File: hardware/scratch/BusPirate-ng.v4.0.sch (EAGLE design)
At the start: 133 parts, among them IC1 IC_MEM_23LC1024, IC10 IC_BUFF_SN74LVC1T45DBV, IC11 IC_BUFF_SN74LVC1T45DBV, IC12 74LVC1G07DBV, IC13 IC_BUFF_SN74LVC1T45DBV, IC14 IC_BL1551, IC15 IC_BL1551, IC16 74HCT4066PW, IC2 IC_MEM_23LC1024, IC3 IC_74AC573, IC4 74LVC1G07DBV, IC5 74LVC1G07DBV, IC6 74LVC1G07DBV, IC7 74LVC1G07DBV, IC8 IC_BUFF_SN74LVC1T45DBV, IC9 IC_BUFF_SN74LVC1T45DBV, J1 CON_HEADER_2X02-PTH, J2 CON_HEADER_1X04, J3 CON_HEADER_1X03-PTH, J4 CON_HEADER_1X10-RIGHT_ANGLED_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, U1 IC_MEM_AT45DB041D, U2 IC_UC_STM32F103ZX, U3 IC_FPGA_ICE40HX4K

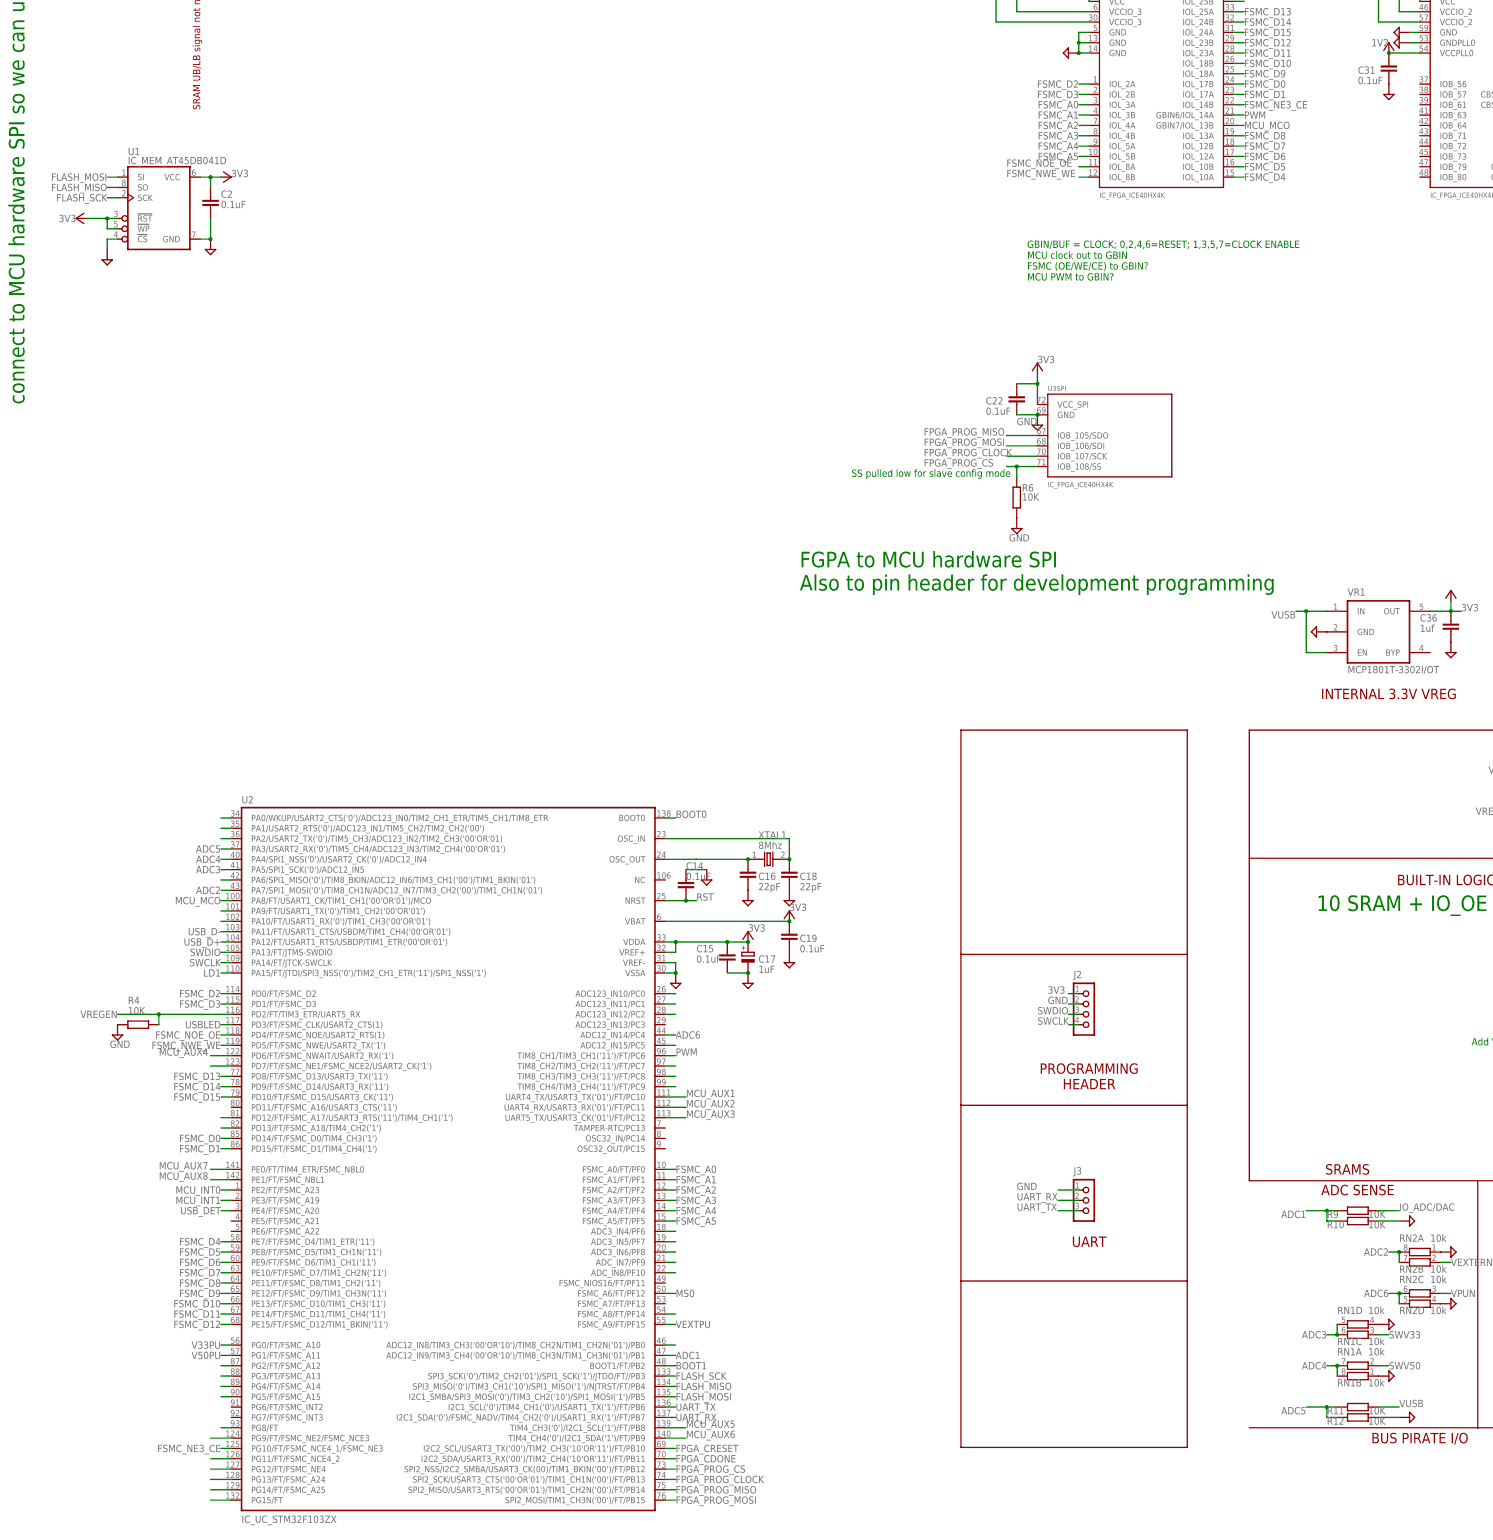
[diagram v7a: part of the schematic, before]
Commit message: added new aux pins connecting MCU to FPGA, created gerbers for BP ultra and BP ultra testboard
Moved pins to make way for AUX pins connection
-swapped MCU pins PB10(FPGA_CRESET) and PB11(FPGA_CDONE)
-moved VREGEN from MCU pin PD2 to PF14

New aux pins connecting MCU to FPGA
-MCU_AUX9 FPGA_37 PF13
-MCU_AUX10 FPGA_38 PB0
-MCU_AUX11 FPGA_39 PC5
-MCU_AUX12 FPGA_41 PA6
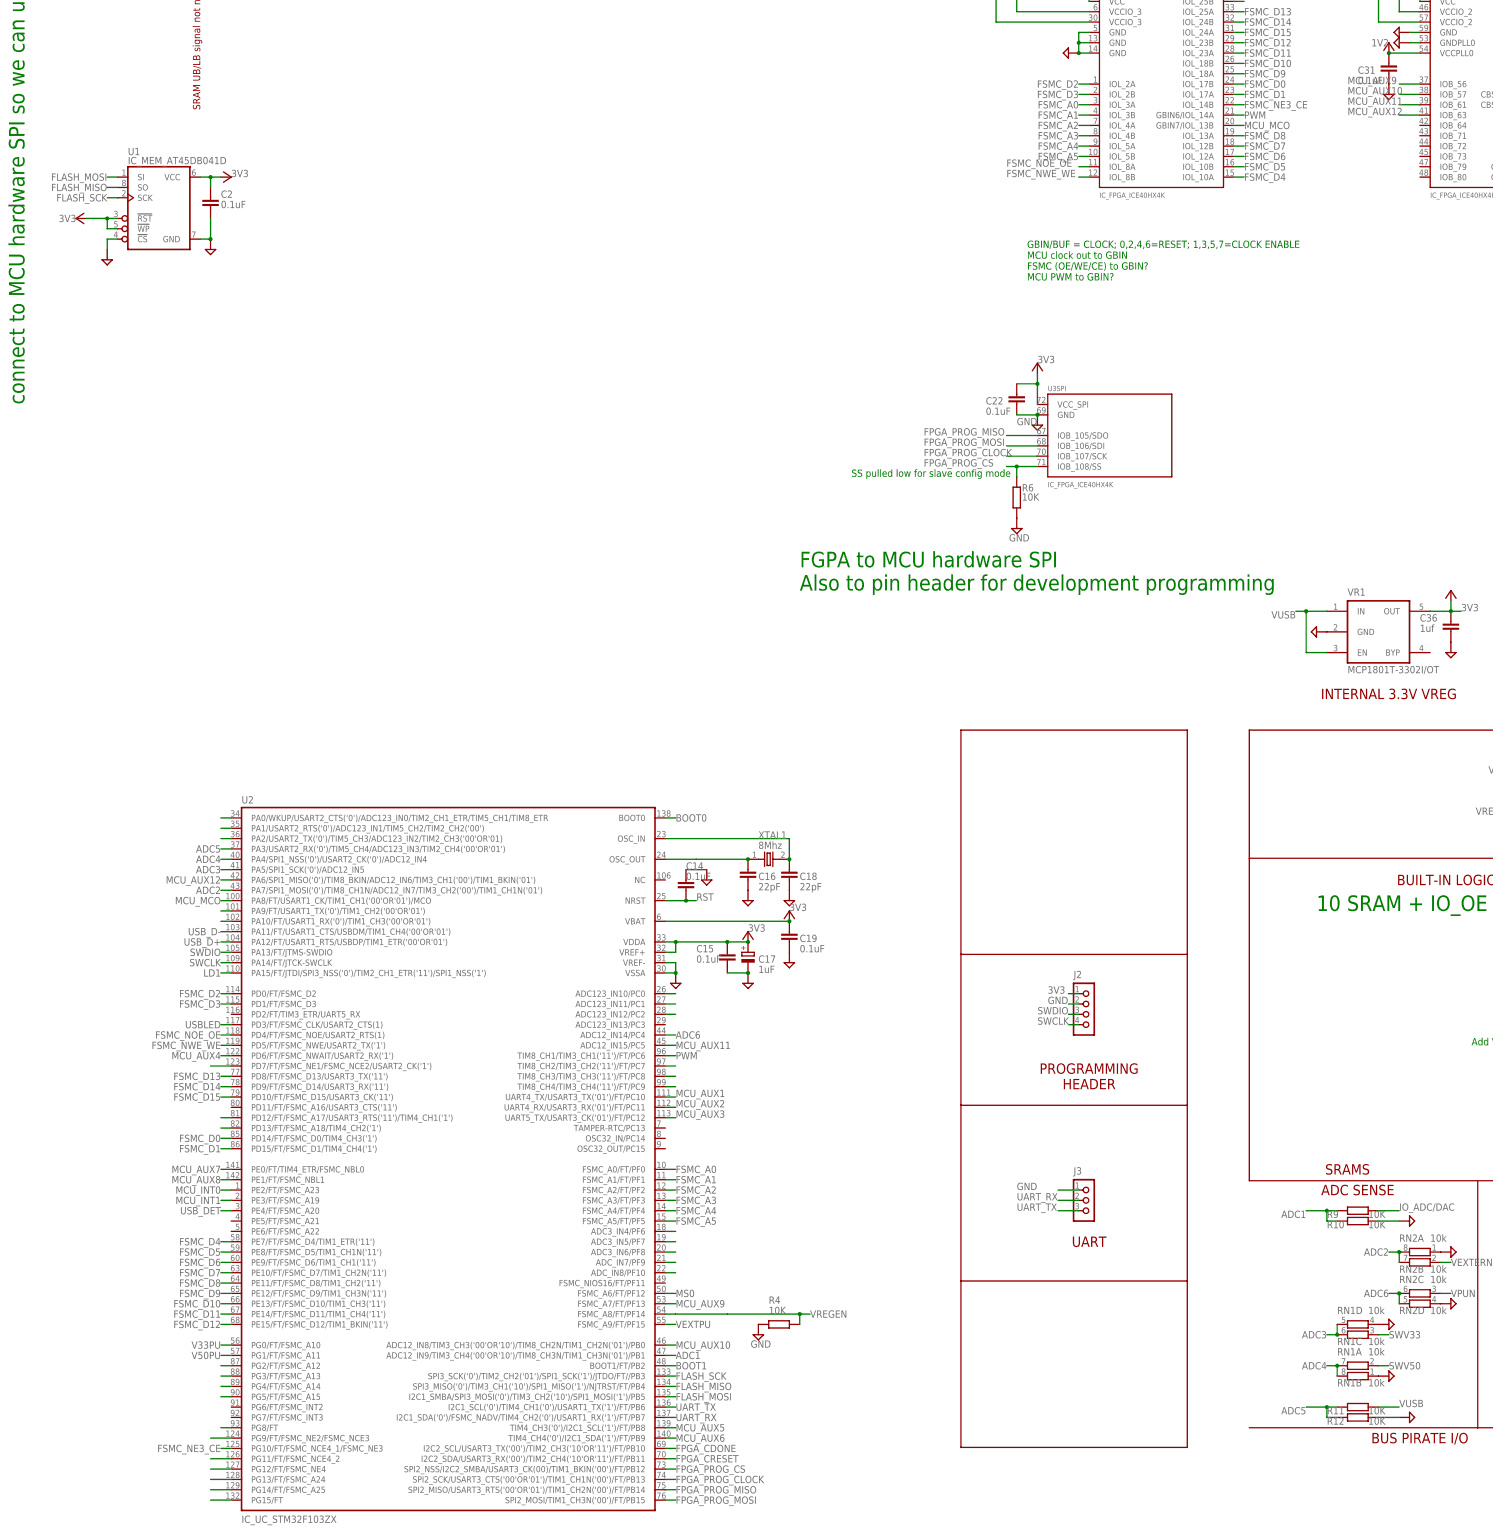
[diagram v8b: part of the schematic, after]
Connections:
- removed net N$15: U2U.FSMC_A8/FT/PF14
- removed net N$25: U2U.ADC12_IN15/PC5
- removed net N$42: U2U.PA6/SPI1_MISO('0')/TIM8_BKIN/ADC12_IN6/TIM3_CH1('00')/TIM1_BKIN('01')
- removed net N$44: U2U.ADC12_IN8/TIM3_CH3('00'OR'10')/TIM8_CH2N/TIM1_CH2N('01')/PB0
- new net MCU_AUX10: U2U.ADC12_IN8/TIM3_CH3('00'OR'10')/TIM8_CH2N/TIM1_CH2N('01')/PB0, U3BANK2.IOB_57
- new net MCU_AUX11: U2U.ADC12_IN15/PC5, U3BANK2.IOB_61
- new net MCU_AUX12: U2U.PA6/SPI1_MISO('0')/TIM8_BKIN/ADC12_IN6/TIM3_CH1('00')/TIM1_BKIN('01'), U3BANK2.IOB_63
- new net MCU_AUX9: U2U.FSMC_A7/FT/PF13, U3BANK2.IOB_56
- net FPGA_CDONE: now also U2U.I2C2_SCL/USART3_TX('00')/TIM2_CH3('10'OR'11')/FT/PB10; no longer U2U.I2C2_SDA/USART3_RX('00')/TIM2_CH4('10'OR'11')/FT/PB11
- net FPGA_CRESET: now also U2U.I2C2_SDA/USART3_RX('00')/TIM2_CH4('10'OR'11')/FT/PB11; no longer U2U.I2C2_SCL/USART3_TX('00')/TIM2_CH3('10'OR'11')/FT/PB10
- net VREGEN: now also U2U.FSMC_A8/FT/PF14; no longer U2U.PD2/FT/TIM3_ETR/UART5_RX
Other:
- moved on the sheet: R4
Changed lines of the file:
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@@
 <instance part="SUPPLY13" gate="GND" x="-121.92" y="149.86" smashed="yes"/>
 <instance part="SUPPLY9" gate="GND" x="-139.7" y="149.86" smashed="yes"/>
-<instance part="R4" gate="G$1" x="-271.78" y="139.7" smashed="yes" rot="R180">
-<attribute name="NAME" x="-274.32" y="144.78" size="1.778" layer="95"/>
-<attribute name="VALUE" x="-274.32" y="142.24" size="1.778" layer="96"/>
+<instance part="R4" gate="G$1" x="-114.3" y="66.04" smashed="yes" rot="R180">
+<attribute name="NAME" x="-116.84" y="71.12" size="1.778" layer="95"/>
+<attribute name="VALUE" x="-116.84" y="68.58" size="1.778" layer="96"/>
 </instance>
-<instance part="SUPPLY5" gate="GND" x="-276.86" y="137.16"/>
+<instance part="SUPPLY5" gate="GND" x="-119.38" y="63.5"/>
 <instance part="J4" gate="J" x="243.84" y="304.8" rot="MR180"/>
 <instance part="C31" gate="G$1" x="35.56" y="373.38" smashed="yes" rot="R180">
@@
 </segment>
 <segment>
-<label x="-276.86" y="142.24" size="1.778" layer="95" align="center-right"/>
+<label x="-106.68" y="68.58" size="1.778" layer="95" align="center-left"/>
 <pinref part="R4" gate="G$1" pin="1"/>
-<wire x1="-266.7" y1="142.24" x2="-276.86" y2="142.24" width="0.1524" layer="91"/>
-<wire x1="-266.7" y1="139.7" x2="-266.7" y2="142.24" width="0.1524" layer="91"/>
-<pinref part="U2" gate="U" pin="PD2/FT/TIM3_ETR/UART5_RX"/>
-<wire x1="-266.7" y1="142.24" x2="-248.92" y2="142.24" width="0.1524" layer="91"/>
-<junction x="-266.7" y="142.24"/>
+<wire x1="-109.22" y1="68.58" x2="-127" y2="68.58" width="0.1524" layer="91"/>
+<wire x1="-109.22" y1="66.04" x2="-109.22" y2="68.58" width="0.1524" layer="91"/>
+<wire x1="-109.22" y1="68.58" x2="-106.68" y2="68.58" width="0.1524" layer="91"/>
+<junction x="-109.22" y="68.58"/>
+<pinref part="U2" gate="U" pin="FSMC_A8/FT/PF14"/>
+<wire x1="-142.24" y1="68.58" x2="-139.7" y2="68.58" width="0.1524" layer="91"/>
+<wire x1="-127" y1="68.58" x2="-139.7" y2="68.58" width="0.1524" layer="91"/>
 </segment>
 </net>
@@
 <pinref part="U2" gate="U" pin="BOOT0"/>
 <wire x1="-142.24" y1="190.5" x2="-139.7" y2="190.5" width="0.1524" layer="91"/>
-<label x="-139.7" y="190.5" size="1.778" layer="95"/>
+<label x="-139.7" y="190.5" size="1.778" layer="95" align="center-left"/>
 </segment>
 </net>
@@
 </segment>
 <segment>
-<pinref part="U2" gate="U" pin="I2C2_SCL/USART3_TX('00')/TIM2_CH3('10'OR'11')/FT/PB10"/>
-<wire x1="-142.24" y1="35.56" x2="-139.7" y2="35.56" width="0.1524" layer="91"/>
-<label x="-139.7" y="35.56" size="1.778" layer="95" align="center-left"/>
+<pinref part="U2" gate="U" pin="I2C2_SDA/USART3_RX('00')/TIM2_CH4('10'OR'11')/FT/PB11"/>
+<wire x1="-142.24" y1="33.02" x2="-139.7" y2="33.02" width="0.1524" layer="91"/>
+<label x="-139.7" y="33.02" size="1.778" layer="95" align="center-left"/>
 </segment>
 </net>
@@
 </segment>
 <segment>
-<pinref part="U2" gate="U" pin="I2C2_SDA/USART3_RX('00')/TIM2_CH4('10'OR'11')/FT/PB11"/>
-<wire x1="-142.24" y1="33.02" x2="-139.7" y2="33.02" width="0.1524" layer="91"/>
-<label x="-139.7" y="33.02" size="1.778" layer="95" align="center-left"/>
+<pinref part="U2" gate="U" pin="I2C2_SCL/USART3_TX('00')/TIM2_CH3('10'OR'11')/FT/PB10"/>
+<wire x1="-142.24" y1="35.56" x2="-139.7" y2="35.56" width="0.1524" layer="91"/>
+<label x="-139.7" y="35.56" size="1.778" layer="95" align="center-left"/>
 </segment>
 </net>
@@
 <pinref part="U2" gate="U" pin="TIM8_CH1/TIM3_CH1('11')/FT/PC6"/>
 <wire x1="-142.24" y1="132.08" x2="-139.7" y2="132.08" width="0.1524" layer="91"/>
-<label x="-139.7" y="132.08" size="1.778" layer="95"/>
+<label x="-139.7" y="132.08" size="1.778" layer="95" align="center-left"/>
 </segment>
 </net>
@@
 <segment>
 <pinref part="U2" gate="U" pin="TIM4_CH4('0')/I2C1_SDA('1')/FT/PB9"/>
-<wire x1="-142.24" y1="38.1" x2="-137.16" y2="38.1" width="0.1524" layer="91"/>
-<label x="-137.16" y="38.1" size="1.778" layer="95"/>
+<wire x1="-142.24" y1="38.1" x2="-139.7" y2="38.1" width="0.1524" layer="91"/>
+<label x="-139.7" y="38.1" size="1.778" layer="95" align="center-left"/>
 </segment>
 </net>
@@
 </segment>
 </net>
-<net name="N$44" class="0">
-<segment>
-<pinref part="U2" gate="U" pin="ADC12_IN8/TIM3_CH3('00'OR'10')/TIM8_CH2N/TIM1_CH2N('01')/PB0"/>
-<wire x1="-142.24" y1="60.96" x2="-139.7" y2="60.96" width="0.1524" layer="91"/>
-</segment>
-</net>
 <net name="N$30" class="0">
 <segment>
@@
 </segment>
 </net>
-<net name="N$42" class="0">
-<segment>
-<pinref part="U2" gate="U" pin="PA6/SPI1_MISO('0')/TIM8_BKIN/ADC12_IN6/TIM3_CH1('00')/TIM1_BKIN('01')"/>
-<wire x1="-248.92" y1="175.26" x2="-251.46" y2="175.26" width="0.1524" layer="91"/>
-</segment>
-</net>
 <net name="N$35" class="0">
 <segment>
@@
 </segment>
 </net>
-<net name="N$25" class="0">
-<segment>
-<pinref part="U2" gate="U" pin="ADC12_IN15/PC5"/>
-<wire x1="-142.24" y1="134.62" x2="-139.7" y2="134.62" width="0.1524" layer="91"/>
-</segment>
-</net>
 <net name="N$24" class="0">
 <segment>
@@
 </segment>
 </net>
-<net name="N$15" class="0">
-<segment>
-<pinref part="U2" gate="U" pin="FSMC_A8/FT/PF14"/>
-<wire x1="-142.24" y1="68.58" x2="-139.7" y2="68.58" width="0.1524" layer="91"/>
-</segment>
-</net>
 <net name="MCU_AUX1" class="0">
 <segment>
 <pinref part="U2" gate="U" pin="UART4_TX/USART3_TX('01')/FT/PC10"/>
-<wire x1="-142.24" y1="121.92" x2="-137.16" y2="121.92" width="0.1524" layer="91"/>
-<label x="-137.16" y="121.92" size="1.778" layer="95"/>
+<wire x1="-142.24" y1="121.92" x2="-139.7" y2="121.92" width="0.1524" layer="91"/>
+<label x="-139.7" y="121.92" size="1.778" layer="95"/>
 </segment>
 <segment>
@@
 <segment>
 <pinref part="U2" gate="U" pin="UART5_TX/USART3_CK('01')/FT/PC12"/>
-<wire x1="-142.24" y1="116.84" x2="-137.16" y2="116.84" width="0.1524" layer="91"/>
-<label x="-137.16" y="116.84" size="1.778" layer="95"/>
+<wire x1="-142.24" y1="116.84" x2="-139.7" y2="116.84" width="0.1524" layer="91"/>
+<label x="-139.7" y="116.84" size="1.778" layer="95"/>
 </segment>
 <segment>
@@
 <segment>
 <pinref part="U2" gate="U" pin="PD6/FT/FSMC_NWAIT/USART2_RX('1')"/>
-<wire x1="-248.92" y1="132.08" x2="-254" y2="132.08" width="0.1524" layer="91"/>
-<label x="-266.7" y="132.08" size="1.778" layer="95"/>
+<wire x1="-248.92" y1="132.08" x2="-251.46" y2="132.08" width="0.1524" layer="91"/>
+<label x="-251.46" y="132.08" size="1.778" layer="95" align="center-right"/>
 </segment>
 <segment>
@@
 <segment>
 <pinref part="U2" gate="U" pin="UART4_RX/USART3_RX('01')/FT/PC11"/>
-<wire x1="-142.24" y1="119.38" x2="-137.16" y2="119.38" width="0.1524" layer="91"/>
-<label x="-137.16" y="119.38" size="1.778" layer="95"/>
+<wire x1="-142.24" y1="119.38" x2="-139.7" y2="119.38" width="0.1524" layer="91"/>
+<label x="-139.7" y="119.38" size="1.778" layer="95"/>
 </segment>
 </net>
@@
 <segment>
 <pinref part="U2" gate="U" pin="TIM4_CH3('0')/I2C1_SCL('1')/FT/PB8"/>
-<wire x1="-142.24" y1="40.64" x2="-137.16" y2="40.64" width="0.1524" layer="91"/>
-<label x="-137.16" y="40.64" size="1.778" layer="95"/>
+<wire x1="-142.24" y1="40.64" x2="-139.7" y2="40.64" width="0.1524" layer="91"/>
+<label x="-139.7" y="40.64" size="1.778" layer="95" align="center-left"/>
 </segment>
 </net>
@@
 <segment>
 <pinref part="U2" gate="U" pin="PE1/FT/FSMC_NBL1"/>
-<wire x1="-248.92" y1="101.6" x2="-254" y2="101.6" width="0.1524" layer="91"/>
-<label x="-266.7" y="101.6" size="1.778" layer="95"/>
+<wire x1="-248.92" y1="101.6" x2="-251.46" y2="101.6" width="0.1524" layer="91"/>
+<label x="-251.46" y="101.6" size="1.778" layer="95" align="center-right"/>
 </segment>
 <segment>
@@
 <segment>
 <pinref part="U2" gate="U" pin="PE0/FT/TIM4_ETR/FSMC_NBL0"/>
-<wire x1="-248.92" y1="104.14" x2="-254" y2="104.14" width="0.1524" layer="91"/>
-<label x="-266.7" y="104.14" size="1.778" layer="95"/>
+<wire x1="-248.92" y1="104.14" x2="-251.46" y2="104.14" width="0.1524" layer="91"/>
+<label x="-251.46" y="104.14" size="1.778" layer="95" align="center-right"/>
 </segment>
 <segment>
@@
 </segment>
 </net>
+<net name="MCU_AUX9" class="0">
+<segment>
+<pinref part="U3" gate="BANK2" pin="IOB_56"/>
+<wire x1="43.18" y1="370.84" x2="38.1" y2="370.84" width="0.1524" layer="91"/>
+<label x="25.4" y="370.84" size="1.778" layer="95"/>
+</segment>
+<segment>
+<pinref part="U2" gate="U" pin="FSMC_A7/FT/PF13"/>
+<wire x1="-142.24" y1="71.12" x2="-139.7" y2="71.12" width="0.1524" layer="91"/>
+<label x="-139.7" y="71.12" size="1.778" layer="95" align="center-left"/>
+</segment>
+</net>
+<net name="MCU_AUX10" class="0">
+<segment>
+<pinref part="U3" gate="BANK2" pin="IOB_57"/>
+<wire x1="43.18" y1="368.3" x2="38.1" y2="368.3" width="0.1524" layer="91"/>
+<label x="25.4" y="368.3" size="1.778" layer="95"/>
+</segment>
+<segment>
+<pinref part="U2" gate="U" pin="ADC12_IN8/TIM3_CH3('00'OR'10')/TIM8_CH2N/TIM1_CH2N('01')/PB0"/>
+<wire x1="-142.24" y1="60.96" x2="-139.7" y2="60.96" width="0.1524" layer="91"/>
+<label x="-139.7" y="60.96" size="1.778" layer="95" align="center-left"/>
+</segment>
+</net>
+<net name="MCU_AUX11" class="0">
+<segment>
+<pinref part="U3" gate="BANK2" pin="IOB_61"/>
+<wire x1="43.18" y1="365.76" x2="38.1" y2="365.76" width="0.1524" layer="91"/>
+<label x="25.4" y="365.76" size="1.778" layer="95"/>
+</segment>
+<segment>
+<pinref part="U2" gate="U" pin="ADC12_IN15/PC5"/>
+<wire x1="-142.24" y1="134.62" x2="-139.7" y2="134.62" width="0.1524" layer="91"/>
+<label x="-139.7" y="134.62" size="1.778" layer="95" align="center-left"/>
+</segment>
+</net>
+<net name="MCU_AUX12" class="0">
+<segment>
+<pinref part="U3" gate="BANK2" pin="IOB_63"/>
+<wire x1="43.18" y1="363.22" x2="38.1" y2="363.22" width="0.1524" layer="91"/>
+<label x="25.4" y="363.22" size="1.778" layer="95"/>
+</segment>
+<segment>
+<pinref part="U2" gate="U" pin="PA6/SPI1_MISO('0')/TIM8_BKIN/ADC12_IN6/TIM3_CH1('00')/TIM1_BKIN('01')"/>
+<wire x1="-248.92" y1="175.26" x2="-251.46" y2="175.26" width="0.1524" layer="91"/>
+<label x="-251.46" y="175.26" size="1.778" layer="95" align="center-right"/>
+</segment>
+</net>
